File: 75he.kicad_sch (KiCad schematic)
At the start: 0 parts

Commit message: start placing mcu capacitor
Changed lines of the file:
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@@
 	)
 	(sheet
-		(at 21.59 139.7)
+		(at 21.59 132.08)
 		(size 53.34 48.26)
 		(exclude_from_sim no)
@@
 		)
 		(property "Sheetname" "Power Supply"
-			(at 21.59 138.9884 0)
+			(at 21.59 131.3684 0)
 			(effects
 				(font
@@
 		)
 		(property "Sheetfile" "power_supply.kicad_sch"
-			(at 21.59 188.5446 0)
+			(at 21.59 180.9246 0)
 			(effects
 				(font

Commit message: compute diff pair spacing
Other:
- note added: "JLC04161H-7628"

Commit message: caca
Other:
- added sheet LED (led.kicad_sch)
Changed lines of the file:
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@@
+	)
+	(sheet
+		(at 231.14 27.94)
+		(size 46.99 39.37)
+		(exclude_from_sim no)
+		(in_bom yes)
+		(on_board yes)
+		(dnp no)
+		(fields_autoplaced yes)
+		(stroke
+			(width 0.1524)
+			(type solid)
+		)
+		(fill
+			(color 0 0 0 0.0000)
+		)
+		(property "Sheetname" "LED"
+			(at 231.14 27.2284 0)
+			(effects
+				(font
+					(size 1.27 1.27)
+				)
+				(justify left bottom)
+			)
+		)
+		(property "Sheetfile" "led.kicad_sch"
+			(at 231.14 67.8946 0)
+			(effects
+				(font
+					(size 1.27 1.27)
+				)
+				(justify left top)
+			)
+		)
+		(instances
+			(project "75he"
+				(path "/0edb4e17-93a4-4f7b-ad91-3a5c72b69d23"
+					(page "7")
+				)
+			)
+		)
 	)
 	(sheet

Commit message: mux placement
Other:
- added sheet Mounting Holes (screws.kicad_sch)
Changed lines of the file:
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@@
+	)
+	(sheet
+		(at 232.41 93.345)
+		(size 42.545 38.1)
+		(exclude_from_sim no)
+		(in_bom yes)
+		(on_board yes)
+		(dnp no)
+		(fields_autoplaced yes)
+		(stroke
+			(width 0.1524)
+			(type solid)
+		)
+		(fill
+			(color 0 0 0 0.0000)
+		)
+		(property "Sheetname" "Mounting Holes"
+			(at 232.41 92.6334 0)
+			(effects
+				(font
+					(size 1.27 1.27)
+				)
+				(justify left bottom)
+			)
+		)
+		(property "Sheetfile" "screws.kicad_sch"
+			(at 232.41 132.0296 0)
+			(effects
+				(font
+					(size 1.27 1.27)
+				)
+				(justify left top)
+			)
+		)
+		(instances
+			(project "75he"
+				(path "/0edb4e17-93a4-4f7b-ad91-3a5c72b69d23"
+					(page "8")
+				)
+			)
+		)
 	)
 	(sheet

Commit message: usb diff pair
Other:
- note added: "USB D+/D- 90 Ohm Trace width = 0.1575mm Trace spacing = 0.2mm JLC06161H-3313A"
- note removed: "JLC04161H-7628"

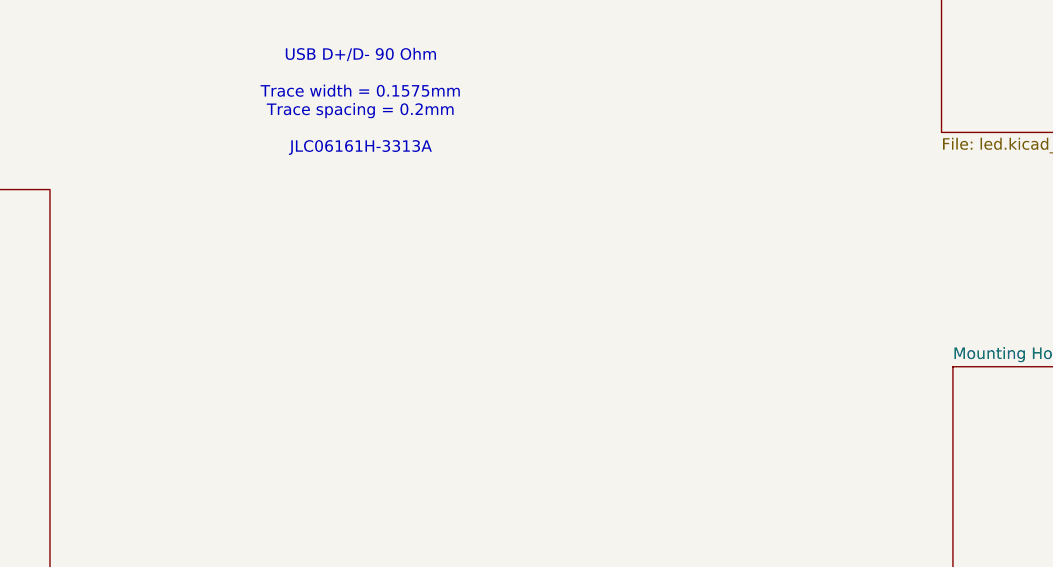
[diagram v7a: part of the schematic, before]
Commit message: add jlc drc & route mux select
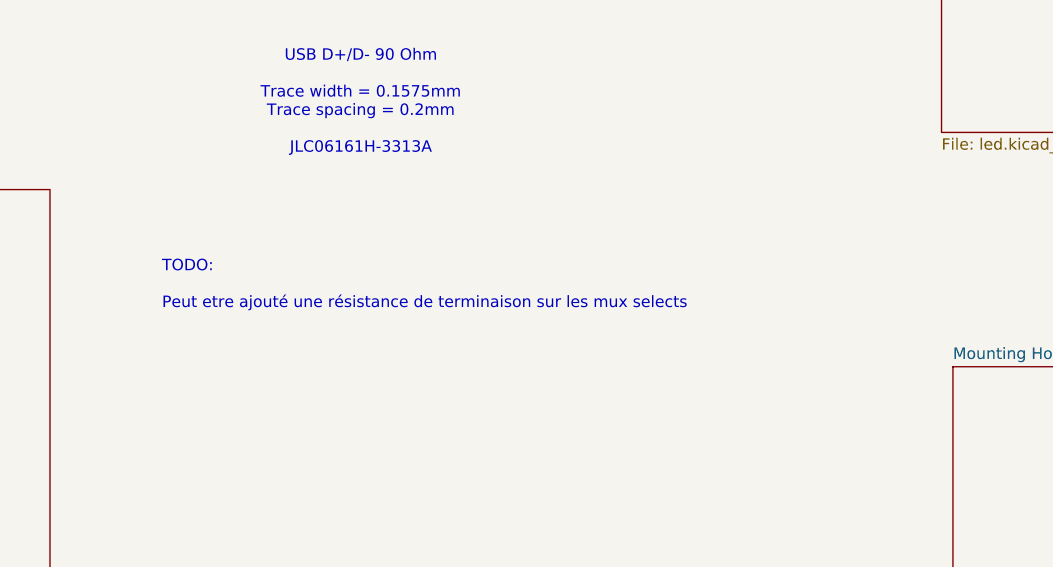
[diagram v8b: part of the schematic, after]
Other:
- note added: "TODO: Peut etre ajouté une résistance de terminaison sur les mux selects"
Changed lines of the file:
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@@
+		)
+	)
+	(text "TODO:\n\nPeut etre ajouté une résistance de terminaison sur les mux selects"
+		(exclude_from_sim no)
+		(at 144.526 84.328 0)
+		(effects
+			(font
+				(size 1.27 1.27)
+			)
+			(justify left)
 		)
 	)
